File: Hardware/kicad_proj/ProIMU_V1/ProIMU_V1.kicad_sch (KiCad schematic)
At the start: 34 parts, among them J1 Conn_02x03_Counter_Clockwise, J4 502570-0893, U1 ADM101E, U2 TJA1051T-3, U4 AIR602, U5 BMP280, U6 MPU-9250, U9 L80-M39

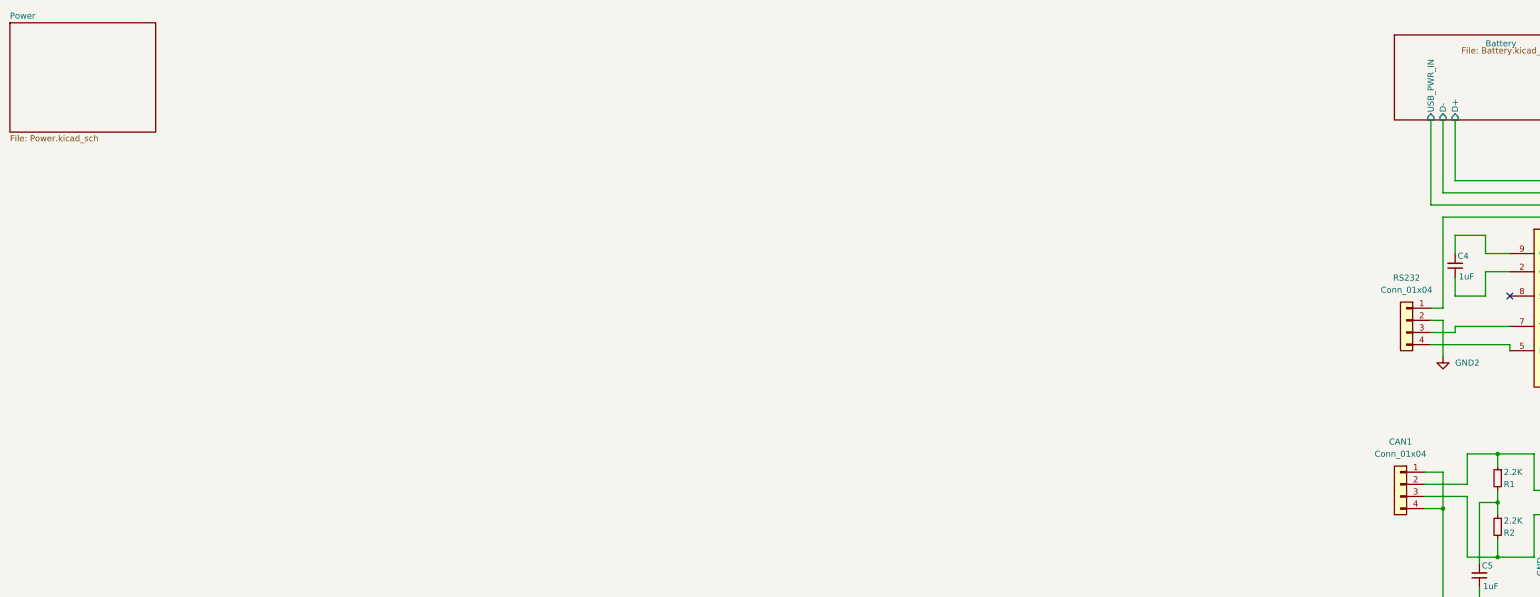
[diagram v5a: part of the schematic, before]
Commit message: Updated schematic. Added new isoalted dc/dc converter. Charger circuit needs to be updated
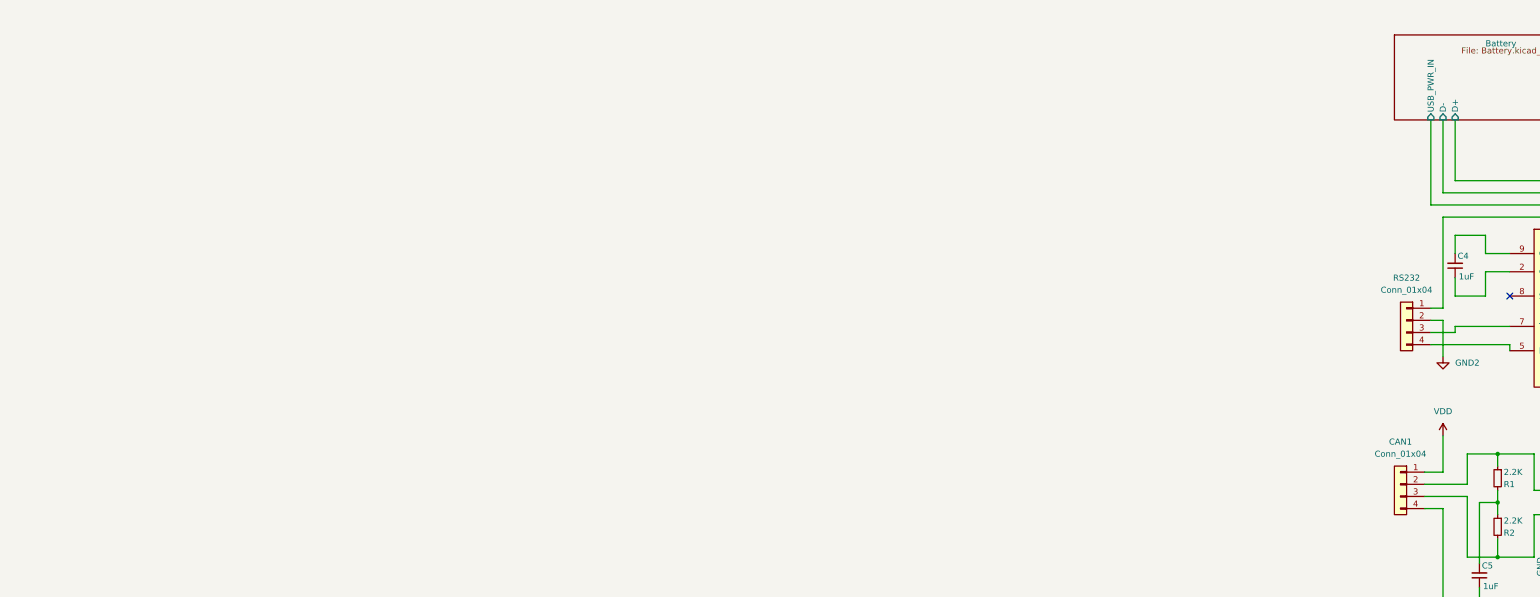
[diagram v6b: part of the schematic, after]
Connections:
- net VDD: now also CAN1.1 (Pin_1)
- net at C5.1, CAN1.4 (Pin_4): no longer CAN1.1 (Pin_1)
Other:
- removed sheet Power
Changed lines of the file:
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@@
   (junction (at 326.39 118.11) (diameter 0) (color 0 0 0 0)
-  )
-  (junction (at 314.96 119.38) (diameter 0) (color 0 0 0 0)
   )
   (junction (at 350.52 132.08) (diameter 0) (color 0 0 0 0)
@@
     (stroke (width 0) (type default) (color 0 0 0 0))
   )
-  (wire (pts (xy 314.96 111.76) (xy 314.96 119.38))
-    (stroke (width 0) (type default) (color 0 0 0 0))
-  )
   (wire (pts (xy 505.46 110.49) (xy 505.46 116.84))
     (stroke (width 0) (type default) (color 0 0 0 0))
@@
   )
   (wire (pts (xy 558.8 40.64) (xy 558.8 39.37))
+    (stroke (width 0) (type default) (color 0 0 0 0))
+  )
+  (wire (pts (xy 314.96 104.14) (xy 314.96 111.76))
     (stroke (width 0) (type default) (color 0 0 0 0))
   )
@@
     )
     (property "Datasheet" "" (id 3) (at 527.05 166.37 0)
+      (effects (font (size 1.27 1.27)) hide)
+    )
+    (pin "1")
+  )
+  (symbol (lib_id "power:VDD") (at 314.96 104.14 0) (unit 1)
+    (in_bom yes) (on_board yes) (fields_autoplaced)
+    (property "Reference" "#PWR?" (id 0) (at 314.96 107.95 0)
+      (effects (font (size 1.27 1.27)) hide)
+    )
+    (property "Value" "VDD" (id 1) (at 314.96 99.06 0))
+    (property "Footprint" "" (id 2) (at 314.96 104.14 0)
+      (effects (font (size 1.27 1.27)) hide)
+    )
+    (property "Datasheet" "" (id 3) (at 314.96 104.14 0)
       (effects (font (size 1.27 1.27)) hide)
     )
@@
     )
   )
-  (sheet (at 15.24 17.78) (size 30.48 22.86) (fields_autoplaced)
-    (stroke (width 0.1524) (type solid) (color 0 0 0 0))
-    (fill (color 0 0 0 0.0000))
-    (property "Sheet name" "Power" (id 0) (at 15.24 17.0684 0)
-      (effects (font (size 1.27 1.27)) (justify left bottom))
-    )
-    (property "Sheet file" "Power.kicad_sch" (id 1) (at 15.24 41.2246 0)
-      (effects (font (size 1.27 1.27)) (justify left top))
-    )
-  )
   (sheet_instances
     (path "/" (page "1"))
     (path "/09535cde-9ba2-41fd-bb26-86cd9c93b7a7" (page "2"))
-    (path "/dee84a73-b9e9-4e07-8db7-0aa14fccfa40" (page "4"))
     (path "/a9803014-b724-4cae-ba4b-6660e60196e3" (page "5"))
   )
@@
       (reference "#PWR040") (unit 1) (value "GND") (footprint "")
     )
-    (path "/dee84a73-b9e9-4e07-8db7-0aa14fccfa40/10b46f6b-0f30-4226-99d0-381c99a4a2d9"
-      (reference "#PWR041") (unit 1) (value "VDD") (footprint "")
-    )
-    (path "/dee84a73-b9e9-4e07-8db7-0aa14fccfa40/63998af5-b817-4ba3-80a2-fb8e017e3bed"
-      (reference "#PWR042") (unit 1) (value "GND") (footprint "")
-    )
-    (path "/dee84a73-b9e9-4e07-8db7-0aa14fccfa40/aaef173f-1148-4aea-a1f5-891df69785f8"
-      (reference "#PWR044") (unit 1) (value "VDD") (footprint "")
-    )
-    (path "/dee84a73-b9e9-4e07-8db7-0aa14fccfa40/e9a96154-da01-4e5e-8bfe-d81ac8273e07"
-      (reference "#PWR045") (unit 1) (value "GND") (footprint "")
-    )
-    (path "/dee84a73-b9e9-4e07-8db7-0aa14fccfa40/6db7da7f-af3b-4506-ae16-7d3c30043925"
-      (reference "#PWR047") (unit 1) (value "GND") (footprint "")
-    )
-    (path "/dee84a73-b9e9-4e07-8db7-0aa14fccfa40/2d0442ce-4083-42c6-9c4f-b06ed816c38b"
-      (reference "#PWR049") (unit 1) (value "+3V3") (footprint "")
-    )
     (path "/a9803014-b724-4cae-ba4b-6660e60196e3/62b78a8b-95a1-49c0-b076-432f44f9a415"
       (reference "#PWR058") (unit 1) (value "+3V3") (footprint "")
@@
       (reference "#PWR0114") (unit 1) (value "GND") (footprint "")
     )
+    (path "/09535cde-9ba2-41fd-bb26-86cd9c93b7a7/0126f431-4462-4e3f-b939-4ec3ae2fedb8"
+      (reference "#PWR?") (unit 1) (value "GND") (footprint "")
+    )
+    (path "/06f66e01-0af5-4067-962a-ab3f70e06c7a"
+      (reference "#PWR?") (unit 1) (value "VDD") (footprint "")
+    )
     (path "/0c260b7f-009c-452c-a58b-377080500162"
       (reference "#PWR?") (unit 1) (value "GND") (footprint "")
     )
+    (path "/09535cde-9ba2-41fd-bb26-86cd9c93b7a7/21ffe51b-3324-4566-82fb-2163e620a1dc"
+      (reference "#PWR?") (unit 1) (value "GND") (footprint "")
+    )
+    (path "/09535cde-9ba2-41fd-bb26-86cd9c93b7a7/4fead911-100b-46f9-afb2-9982562942e5"
+      (reference "#PWR?") (unit 1) (value "GND") (footprint "")
+    )
+    (path "/09535cde-9ba2-41fd-bb26-86cd9c93b7a7/54027b66-62fe-4828-88d9-d5465542d107"
+      (reference "#PWR?") (unit 1) (value "GND") (footprint "")
+    )
+    (path "/09535cde-9ba2-41fd-bb26-86cd9c93b7a7/8110de98-13ea-4e67-8948-3715ca648761"
+      (reference "#PWR?") (unit 1) (value "+3V3") (footprint "")
+    )
+    (path "/09535cde-9ba2-41fd-bb26-86cd9c93b7a7/9bfa9aa5-5b50-4929-be1d-d491ba7ef3c8"
+      (reference "#PWR?") (unit 1) (value "VDD") (footprint "")
+    )
+    (path "/09535cde-9ba2-41fd-bb26-86cd9c93b7a7/a4afb600-cc22-4077-8d37-312922c9cf00"
+      (reference "#PWR?") (unit 1) (value "GND1") (footprint "")
+    )
+    (path "/09535cde-9ba2-41fd-bb26-86cd9c93b7a7/cd42a12b-4c1f-4382-9bbc-31604528599a"
+      (reference "#PWR?") (unit 1) (value "GND") (footprint "")
+    )
+    (path "/09535cde-9ba2-41fd-bb26-86cd9c93b7a7/dbd59ba2-5b71-4054-8306-3c08cce1166e"
+      (reference "#PWR?") (unit 1) (value "+5V") (footprint "")
+    )
+    (path "/09535cde-9ba2-41fd-bb26-86cd9c93b7a7/fcba2812-a592-489c-b388-094c7707140a"
+      (reference "#PWR?") (unit 1) (value "GND1") (footprint "")
+    )
     (path "/09535cde-9ba2-41fd-bb26-86cd9c93b7a7/e67f3a4a-b4bb-4b38-a7f4-b0011cb79e12"
       (reference "BAT1") (unit 1) (value "Conn_01x02") (footprint "Connector_PinSocket_2.54mm:PinSocket_1x02_P2.54mm_Vertical")
@@
       (reference "C11") (unit 1) (value "10nF") (footprint "Capacitor_SMD:C_0402_1005Metric_Pad0.74x0.62mm_HandSolder")
     )
-    (path "/dee84a73-b9e9-4e07-8db7-0aa14fccfa40/687c1784-7a62-4ed0-861d-7d7d5b418cca"
-      (reference "C12") (unit 1) (value "1uF") (footprint "Capacitor_SMD:C_0402_1005Metric_Pad0.74x0.62mm_HandSolder")
-    )
-    (path "/dee84a73-b9e9-4e07-8db7-0aa14fccfa40/56b062b9-0eec-476c-a7a8-6a7c41dcf8e3"
-      (reference "C14") (unit 1) (value "1uF") (footprint "Capacitor_SMD:C_0402_1005Metric_Pad0.74x0.62mm_HandSolder")
-    )
     (path "/a9803014-b724-4cae-ba4b-6660e60196e3/a41a265d-c512-4dcd-a7ac-4e6b99b20466"
       (reference "C16") (unit 1) (value "1uF") (footprint "Capacitor_SMD:C_0402_1005Metric_Pad0.74x0.62mm_HandSolder")
@@
       (reference "C29") (unit 1) (value "1uF") (footprint "Capacitor_SMD:C_0402_1005Metric_Pad0.74x0.62mm_HandSolder")
     )
+    (path "/09535cde-9ba2-41fd-bb26-86cd9c93b7a7/0e47259d-a268-4b91-abf1-8572a42941da"
+      (reference "C?") (unit 1) (value "C") (footprint "")
+    )
+    (path "/09535cde-9ba2-41fd-bb26-86cd9c93b7a7/2fb58f00-b13d-4735-aba4-3438f7ac4400"
+      (reference "C?") (unit 1) (value "C") (footprint "")
+    )
+    (path "/09535cde-9ba2-41fd-bb26-86cd9c93b7a7/95b98ec8-c481-4fea-b969-2f561d996151"
+      (reference "C?") (unit 1) (value "C") (footprint "")
+    )
+    (path "/09535cde-9ba2-41fd-bb26-86cd9c93b7a7/a6405b30-7208-409a-ac08-671a1d732c90"
+      (reference "C?") (unit 1) (value "C") (footprint "")
+    )
     (path "/3e0eb4b9-74c1-441d-add2-8f7583266e9e"
       (reference "CAN1") (unit 1) (value "Conn_01x04") (footprint "Connector_JST:JST_PH_S4B-PH-SM4-TB_1x04-1MP_P2.00mm_Horizontal")
@@
       (reference "J4") (unit 1) (value "502570-0893") (footprint "footprints:MOLEX_502570-0893")
     )
-    (path "/dee84a73-b9e9-4e07-8db7-0aa14fccfa40/0eaff48a-8e4b-4b66-8d68-868c31147796"
-      (reference "L1") (unit 1) (value "INDUCTOR") (footprint "")
-    )
     (path "/09535cde-9ba2-41fd-bb26-86cd9c93b7a7/0226f9d9-7549-4f34-a5fc-64756f504418"
       (reference "L3") (unit 1) (value "1.0uH") (footprint "Inductor_SMD:L_0805_2012Metric_Pad1.05x1.20mm_HandSolder")
     )
+    (path "/09535cde-9ba2-41fd-bb26-86cd9c93b7a7/6694b787-930c-4b46-b4e9-fe5cdc8d4b6e"
+      (reference "PS?") (unit 1) (value "PDP1-S5-S5-M-TR") (footprint "footprints:CONV_PDP1-S5-S5-M-TR")
+    )
     (path "/09535cde-9ba2-41fd-bb26-86cd9c93b7a7/6c3ce01a-e542-4d43-974f-484d11a56774"
       (reference "Q1") (unit 1) (value "2SC4213") (footprint "Package_TO_SOT_SMD:SOT-323_SC-70")
@@
       (reference "R6") (unit 1) (value "2.2K") (footprint "Resistor_SMD:R_0402_1005Metric_Pad0.72x0.64mm_HandSolder")
     )
-    (path "/dee84a73-b9e9-4e07-8db7-0aa14fccfa40/2aee96ad-a0f9-45cb-b669-2540f95da0fb"
-      (reference "R7") (unit 1) (value "10K") (footprint "Resistor_SMD:R_0402_1005Metric_Pad0.72x0.64mm_HandSolder")
-    )
-    (path "/dee84a73-b9e9-4e07-8db7-0aa14fccfa40/ad385196-5552-4b2d-8e83-43d7853e0ed9"
-      (reference "R8") (unit 1) (value "10K") (footprint "Resistor_SMD:R_0402_1005Metric_Pad0.72x0.64mm_HandSolder")
-    )
     (path "/a9803014-b724-4cae-ba4b-6660e60196e3/8d7a5e13-f924-453a-b239-94af886ade59"
       (reference "R11") (unit 1) (value "10K") (footprint "Resistor_SMD:R_0402_1005Metric_Pad0.72x0.64mm_HandSolder")
@@
       (reference "RS232") (unit 1) (value "Conn_01x04") (footprint "Connector_JST:JST_PH_S4B-PH-SM4-TB_1x04-1MP_P2.00mm_Horizontal")
     )
-    (path "/dee84a73-b9e9-4e07-8db7-0aa14fccfa40/90d7cc19-b5a9-4691-8a0d-947376808099"
-      (reference "SW1") (unit 1) (value "SW_SPDT") (footprint "")
-    )
     (path "/e4b948e8-dd69-48ec-87c4-eb7f4a8970ff"
       (reference "U1") (unit 1) (value "ADM101E") (footprint "Package_SO:MSOP-10_3x3mm_P0.5mm")
@@
       (reference "U6") (unit 1) (value "MPU-9250") (footprint "QFN40P300X300X105-24N")
     )
-    (path "/dee84a73-b9e9-4e07-8db7-0aa14fccfa40/d5e4e418-1e02-4060-989d-745076737cee"
-      (reference "U7") (unit 1) (value "TPS54308") (footprint "Package_TO_SOT_SMD:SOT-23-6")
-    )
     (path "/4e1566a2-d0dc-4fdf-b0f1-889c94702f58"
       (reference "U9") (unit 1) (value "L80-M39") (footprint "footprints:XCVR_L80-M39")
@@
       (reference "U10") (unit 1) (value "STM32F412RETx") (footprint "Package_QFP:LQFP-64_10x10mm_P0.5mm")
     )
+    (path "/09535cde-9ba2-41fd-bb26-86cd9c93b7a7/0facf723-c2b6-4a19-95cc-8d537b176d06"
+      (reference "U?") (unit 1) (value "SPX2920M3-3.3_SOT223") (footprint "Package_TO_SOT_SMD:SOT-223-3_TabPin2")
+    )
     (path "/a762757f-b15c-42b2-bc8c-8dd1f32cb2d2"

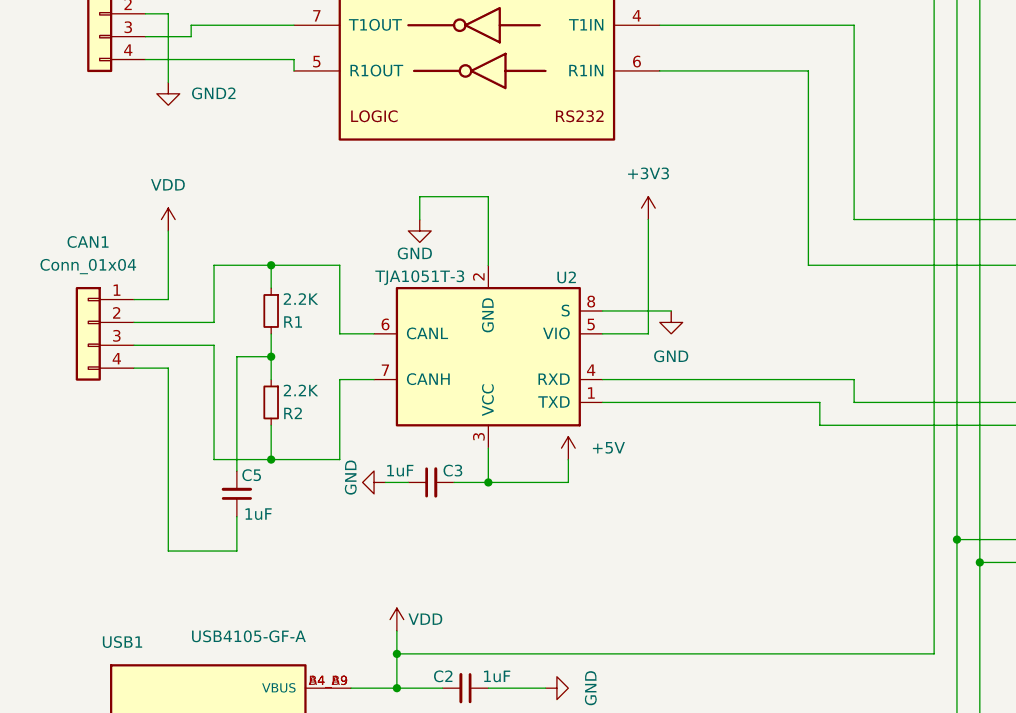
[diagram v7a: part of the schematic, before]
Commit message: Updated schematic and layout
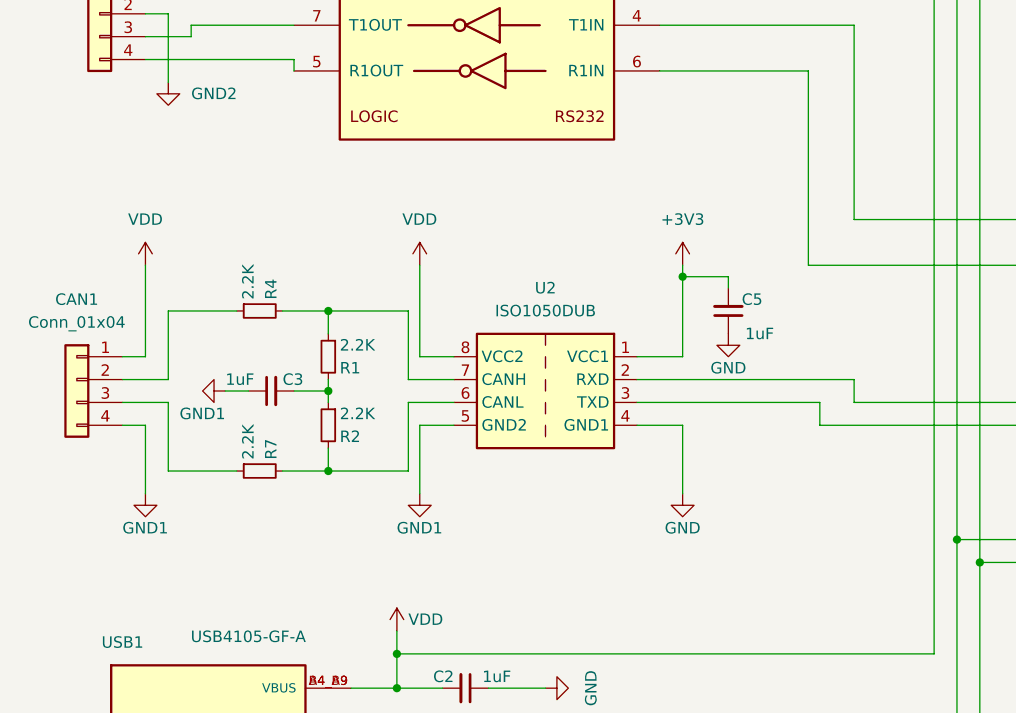
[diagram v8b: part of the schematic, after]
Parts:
- removed U2: TJA1051T-3, Package_SO:SOIC-8_3.9x4.9mm_P1.27mm, symbol Interface_CAN_LIN:TJA1051T-3
- added R4, R7: 2.2K, Resistor_SMD:R_0402_1005Metric_Pad0.72x0.64mm_HandSolder, symbol Device:R_Small
- added U2: ISO1050DUB, Package_SO:SOP-8_6.62x9.15mm_P2.54mm, symbol Interface_CAN_LIN:ISO1050DUB
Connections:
- net +3V3: now also C5.2, U2.1 (VCC1)
- net +5V: no longer C3.2
- net GND: now also C5.1, U2.4 (GND1); no longer C3.1
- net MCU/CAN1_RX: now also U2.2 (RXD)
- net MCU/CAN1_TX: now also U2.3 (TXD)
- net VDD: now also U2.8 (VCC2)
- net at R1.1: now also R4.2, U2.7 (CANH); no longer CAN1.2 (Pin_2)
- net at R1.2, R2.1: now also C3.2; no longer C5.2
- net at R2.2: now also R7.2, U2.6 (CANL); no longer CAN1.3 (Pin_3)
- net GND1: now reaches CAN1.4 (Pin_4)
- net GND1: now also C3.1, U2.5 (GND2); no longer C5.1
- new net: CAN1.2 (Pin_2), R4.1
- new net: CAN1.3 (Pin_3), R7.1
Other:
- moved on the sheet: C3, CAN1, R1, R2
